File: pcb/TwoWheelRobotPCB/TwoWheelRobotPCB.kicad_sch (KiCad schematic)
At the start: 26 parts, among them J1 Motor1, J2 Motor2, U1 NodeMCU1.0(ESP-12E), U2 L298HN, U3 ACS712xLCTR-05B

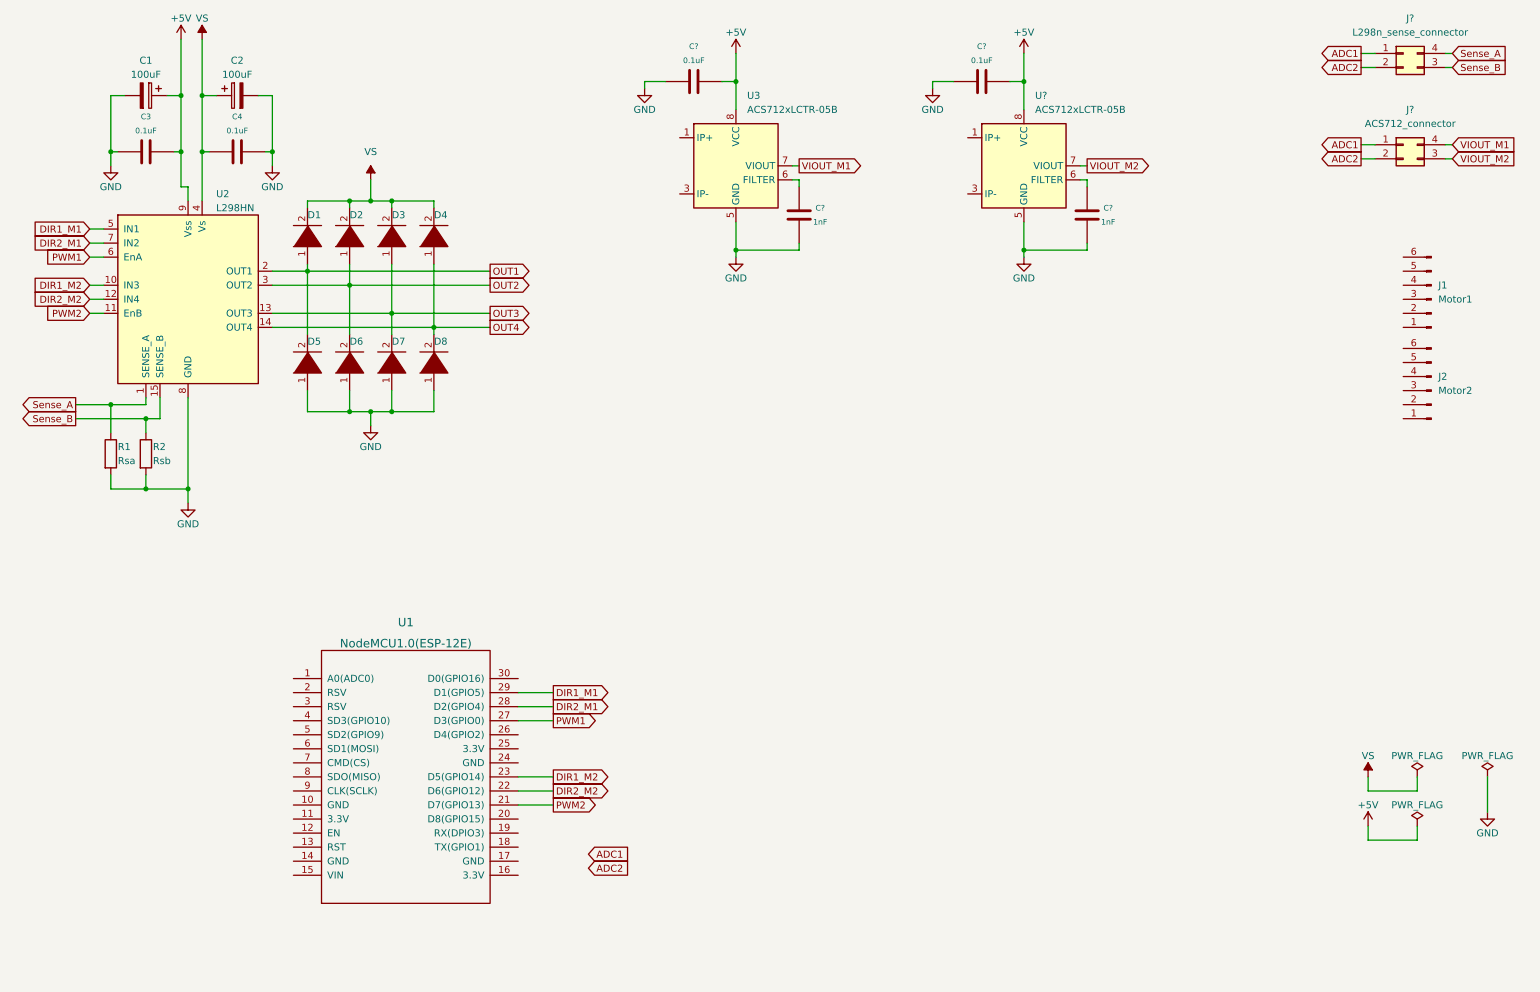
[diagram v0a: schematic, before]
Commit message: robotView class && update pcb
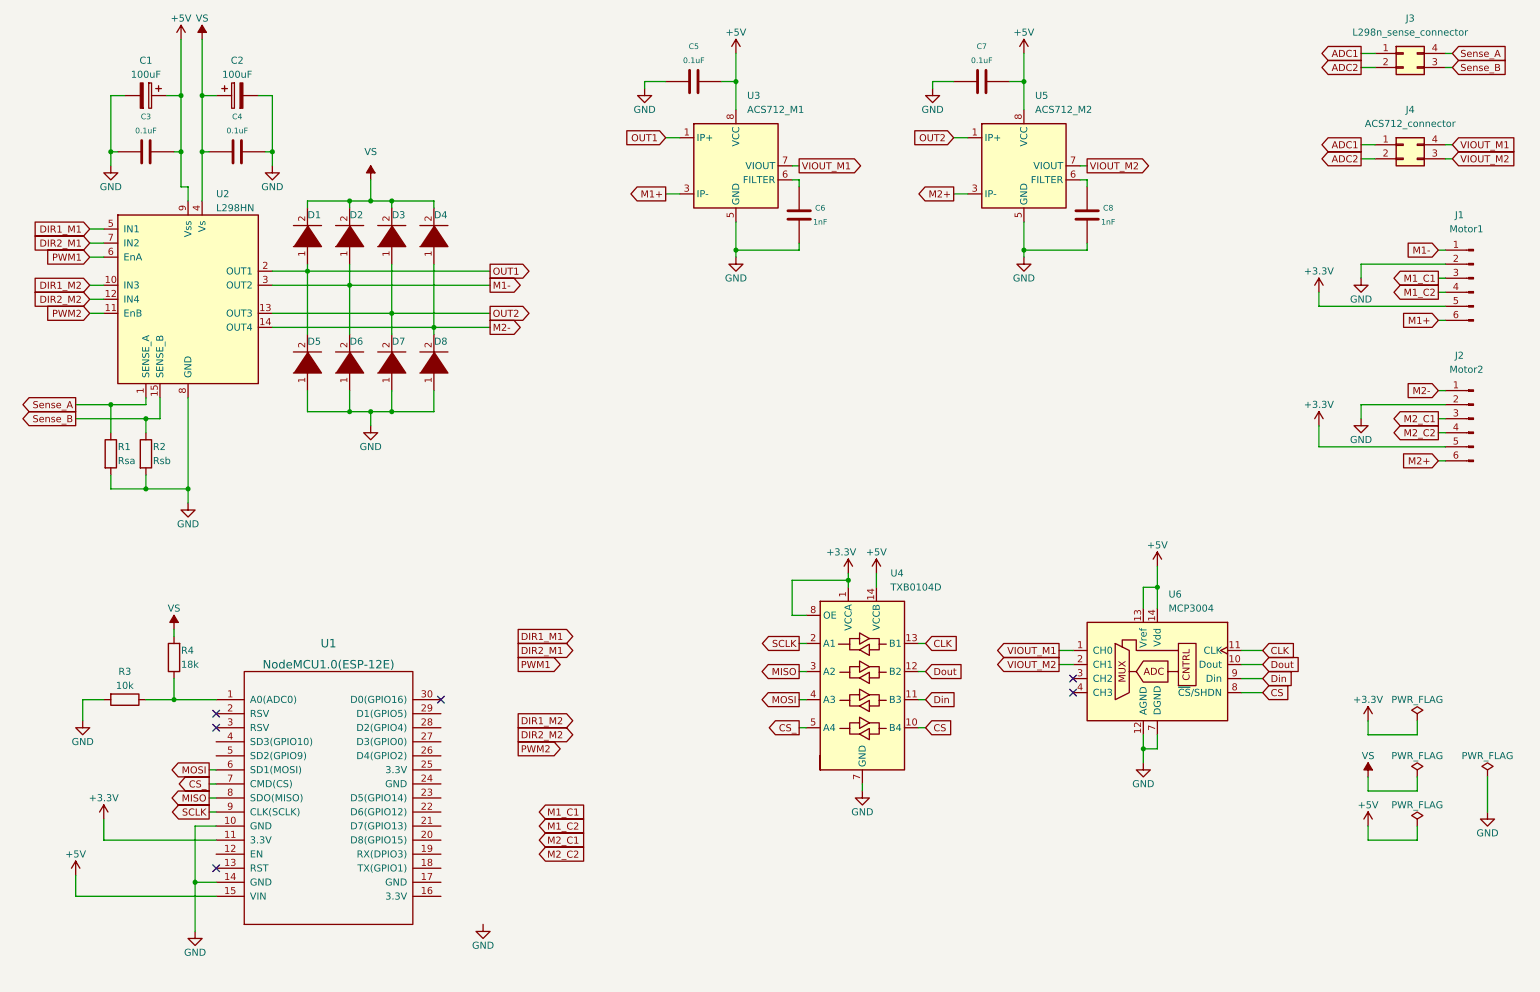
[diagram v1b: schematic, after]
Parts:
- added R3: 10k, symbol Device:R
- added R4: 18k, symbol Device:R
- added U4: TXB0104D, Package_SO:SOIC-14_3.9x8.7mm_P1.27mm, symbol Logic_LevelTranslator:TXB0104D
- added U6: MCP3004, symbol Analog_ADC:MCP3004
- U3: value ACS712xLCTR-05B -> ACS712_M1
- U5: renamed from U?; value ACS712xLCTR-05B -> ACS712_M2
- gave numbers to parts that had none: 6
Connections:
- net OUT3 is gone; now on net OUT2: D3.1 (K), D7.2 (A), U2.13 (OUT3)
- net OUT4 is gone; now on net M2-: D4.1 (K), D8.2 (A), U2.14 (OUT4)
- net +5V: now also U1.15 (VIN), U4.14 (VCCB), U6.13 (Vref), U6.14 (Vdd)
- net DIR1_M1: no longer U1.29 (D1(GPIO5))
- net DIR1_M2: no longer U1.23 (D5(GPIO14))
- net DIR2_M1: no longer U1.28 (D2(GPIO4))
- net DIR2_M2: no longer U1.22 (D6(GPIO12))
- net GND: now also J1.2 (Pin_2), J2.2 (Pin_2), U1.10 (GND), U1.14 (GND), R3.2, U4.7 (GND), U6.12 (AGND), U6.7 (DGND)
- net OUT1: now also U3.1 (IP+), U3.2 (IP+)
- net OUT2: now also U5.1 (IP+), U5.2 (IP+); no longer D2.1 (K), D6.2 (A), U2.3 (OUT2)
- net PWM1: no longer U1.27 (D3(GPIO0))
- net PWM2: no longer U1.21 (D7(GPIO13))
- net VIOUT_M1: now also U6.1 (CH0)
- net VIOUT_M2: now also U6.2 (CH1)
- net VS: now also R4.2
- net at U1.1 (A0(ADC0)): now also R3.1, R4.1
- net +3V3: now reaches U1.11 (3.3V)
- net +3V3: now also J1.5 (Pin_5), J2.5 (Pin_5), U4.1 (VCCA), U4.8 (OE)
- net MOSI: now reaches U1.6 (SD1(MOSI))
- net MOSI: now also U4.4 (A3)
- net CS_: now reaches U1.7 (CMD(CS))
- net CS_: now also U4.5 (A4)
- net MISO: now reaches U1.8 (SDO(MISO))
- net MISO: now also U4.3 (A2)
- net SCLK: now reaches U1.9 (CLK(SCLK))
- net SCLK: now also U4.2 (A1)
- net M2+: now reaches U5.3 (IP-), U5.4 (IP-)
- net M2+: now also J2.6 (Pin_6)
- net M1-: now reaches J1.1 (Pin_1)
- net M1-: now also D2.1 (K), D6.2 (A), U2.3 (OUT2)
- net M1_C1: now reaches J1.3 (Pin_3)
- net M1_C2: now reaches J1.4 (Pin_4)
- net M1+: now reaches J1.6 (Pin_6)
- net M1+: now also U3.3 (IP-), U3.4 (IP-)
- net M2-: now reaches J2.1 (Pin_1)
- net M2_C1: now reaches J2.3 (Pin_3)
- net M2_C2: now reaches J2.4 (Pin_4)
- new net CLK: U4.13 (B1), U6.11 (CLK)
- new net CS: U4.10 (B4), U6.8 (~{CS}/SHDN)
- new net Din: U4.11 (B3), U6.9 (Din)
- new net Dout: U4.12 (B2), U6.10 (Dout)
- no-connect marks 0 -> 6
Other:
- moved on the sheet: J1, J2, U1

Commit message: pcb update
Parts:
- removed C1, C2: 100uF, symbol Device:C_Polarized
- removed C3, C4, C5, C7: 0.1uF, symbol cyclophone:C
- removed C6, C8: 1nF, symbol cyclophone:C
- removed D1, D2, D3, D4, D5, D6, D7, D8: DIODE, symbol pspice:DIODE
- removed J1: Motor1, Connector_PinHeader_2.54mm:PinHeader_1x06_P2.54mm_Vertical, symbol Connector:Conn_01x06_Male
- removed J2: Motor2, Connector_PinHeader_2.54mm:PinHeader_1x06_P2.54mm_Vertical, symbol Connector:Conn_01x06_Male
- removed J3: L298n_sense_connector, Connector_PinHeader_2.54mm:PinHeader_2x02_P2.54mm_Vertical, symbol Connector_Generic:Conn_02x02_Counter_Clockwise
- removed J4: ACS712_connector, Connector_PinHeader_2.54mm:PinHeader_2x02_P2.54mm_Vertical, symbol Connector_Generic:Conn_02x02_Counter_Clockwise
- removed R1: Rsa, symbol Device:R
- removed R2: Rsb, symbol Device:R
- removed U2: L298HN, Package_TO_SOT_THT:TO-220-15_P2.54x2.54mm_StaggerOdd_Lead4.58mm_Vertical, symbol Driver_Motor:L298HN
- removed U3: ACS712_M1, Package_SO:SOIC-8_3.9x4.9mm_P1.27mm, symbol Sensor_Current:ACS712xLCTR-05B
- removed U4: TXB0104D, Package_SO:SOIC-14_3.9x8.7mm_P1.27mm, symbol Logic_LevelTranslator:TXB0104D
- removed U5: ACS712_M2, Package_SO:SOIC-8_3.9x4.9mm_P1.27mm, symbol Sensor_Current:ACS712xLCTR-05B
- removed U6: MCP3004, symbol Analog_ADC:MCP3004
- R3, R4: footprint (none) -> Resistor_SMD:R_0805_2012Metric
- U1: footprint (none) -> NodemcuESP8266_footprint:MODULE_ZC563900
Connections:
- net +3V3: now also U1.16 (3.3V), U1.25 (3.3V)
- net GND: now also U1.17 (GND), U1.24 (GND)
- net M1_C1: now also U1.22 (D6(GPIO12))
- net M1_C2: now also U1.23 (D5(GPIO14))
- net M2_C1: now also U1.21 (D7(GPIO13))
- net M2_C2: now also U1.20 (D8(GPIO15))
- net pwm2: now reaches U1.26 (D4(GPIO2))
- net pwm1: now reaches U1.27 (D3(GPIO0))
- net SDA: now reaches U1.28 (D2(GPIO4))
- net SCL: now reaches U1.29 (D1(GPIO5))
- no-connect marks 6 -> 9
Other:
- added sheet Measurement (Measurement.kicad_sch)
- added sheet MotorDriver (MotorDriver.kicad_sch)
- added sheet Supply (Supply.kicad_sch)
- moved on the sheet: R3, R4, U1

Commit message: update pcb
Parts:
- removed U1: NodeMCU1.0(ESP-12E), NodemcuESP8266_footprint:MODULE_ZC563900, symbol ESP8266:NodeMCU1.0(ESP-12E)
- added U1: ZC563900, NodemcuESP8266_footprint:MODULE_ZC563900, symbol NodemcuV2:ZC563900
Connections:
- net +3V3: now also U1.11 (3V3), U1.16 (3V3), U1.25 (3V3)
- net CS_: now also U1.7 (CMD)
- net GND: now also U1.10 (GND), U1.14 (GND), U1.17 (GND), U1.24 (GND)
- net M1_C1: now also U1.22 (D6)
- net M1_C2: now also U1.23 (D5)
- net M2_C1: now also U1.21 (D7)
- net M2_C2: now also U1.20 (D8)
- net MISO: now also U1.8 (SD0)
- net MOSI: now also U1.6 (SD1)
- net SCL: now also U1.29 (D1)
- net SCLK: now also U1.9 (CLK)
- net SDA: now also U1.28 (D2)
- net VS: now also U1.15 (VIN)
- net pwm1: now also U1.27 (D3)
- net pwm2: now also U1.26 (D4)
- net at R3.1, R4.1: now also U1.1 (A0)
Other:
- moved on the sheet: R3, R4

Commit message: pcb
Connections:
- net pwm1 renamed pwm1_3v3
- net pwm2 renamed pwm2_3v3
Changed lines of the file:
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@@
     )
   )
-  (global_label "pwm2" (shape output) (at 111.76 69.85 0) (fields_autoplaced)
+  (global_label "pwm2_3v3" (shape output) (at 111.76 69.85 0) (fields_autoplaced)
     (effects (font (size 1.27 1.27)) (justify left))
-    (property "Intersheet References" "${INTERSHEET_REFS}" (id 0) (at 119.5555 69.7706 0)
+    (property "Intersheet References" "${INTERSHEET_REFS}" (id 0) (at 123.9098 69.7706 0)
       (effects (font (size 1.27 1.27)) (justify left) hide)
     )
@@
     )
   )
-  (global_label "pwm1" (shape output) (at 111.76 67.31 0) (fields_autoplaced)
+  (global_label "pwm1_3v3" (shape output) (at 111.76 67.31 0) (fields_autoplaced)
     (effects (font (size 1.27 1.27)) (justify left))
-    (property "Intersheet References" "${INTERSHEET_REFS}" (id 0) (at 119.5555 67.2306 0)
+    (property "Intersheet References" "${INTERSHEET_REFS}" (id 0) (at 123.9098 67.2306 0)
       (effects (font (size 1.27 1.27)) (justify left) hide)
     )
@@
       (reference "#FLG04") (unit 1) (value "PWR_FLAG") (footprint "")
     )
+    (path "/7d587865-2231-4a38-9d8a-97d485f2f4e4/4c8df18d-77ed-4411-bc03-a1485170a702"
+      (reference "#PWR01") (unit 1) (value "VS") (footprint "")
+    )
     (path "/a80922d8-842d-4acc-a603-f8902aa0c0c5"
       (reference "#PWR02") (unit 1) (value "GND") (footprint "")
     )
+    (path "/7d587865-2231-4a38-9d8a-97d485f2f4e4/984e7252-4d51-4e18-8cfd-d20f5368238e"
+      (reference "#PWR03") (unit 1) (value "GND") (footprint "")
+    )
+    (path "/7d587865-2231-4a38-9d8a-97d485f2f4e4/cbc1633b-2edb-4841-a64c-00ea63fa9a87"
+      (reference "#PWR04") (unit 1) (value "VS") (footprint "")
+    )
     (path "/bab16bbd-be5b-4ff6-9805-0a16f023b621"
       (reference "#PWR05") (unit 1) (value "VS") (footprint "")
     )
+    (path "/7d587865-2231-4a38-9d8a-97d485f2f4e4/df76744a-2672-4df3-b0f1-8632a1e0c956"
+      (reference "#PWR06") (unit 1) (value "GND") (footprint "")
+    )
+    (path "/7d587865-2231-4a38-9d8a-97d485f2f4e4/15eb6ae6-6d8f-499f-a0b3-7ad0e61d54f9"
+      (reference "#PWR07") (unit 1) (value "GND") (footprint "")
+    )
     (path "/5d98914d-1801-43c8-96ca-19f222dbae40/43f9481c-710c-4a70-b5b4-8f4b24641629"
       (reference "#PWR08") (unit 1) (value "GND") (footprint "")
@@
       (reference "#PWR011") (unit 1) (value "VS") (footprint "")
     )
+    (path "/7d587865-2231-4a38-9d8a-97d485f2f4e4/d045e7ba-b7a5-4eb8-ba31-1a87a3b8ae7d"
+      (reference "#PWR012") (unit 1) (value "+5V") (footprint "")
+    )
     (path "/5d98914d-1801-43c8-96ca-19f222dbae40/30c9f8d1-6270-4c18-a2b6-c43a30582ae1"
       (reference "#PWR013") (unit 1) (value "GND") (footprint "")
@@
       (reference "#PWR019") (unit 1) (value "GND") (footprint "")
     )
-    (path "/5d98914d-1801-43c8-96ca-19f222dbae40/47165815-d55a-454b-961f-9380e65de16a"
+    (path "/5d98914d-1801-43c8-96ca-19f222dbae40/e3cbd370-7c22-4222-878e-9ad9b35baaf2"
       (reference "#PWR020") (unit 1) (value "+3.3V") (footprint "")
     )
-    (path "/5d98914d-1801-43c8-96ca-19f222dbae40/e457ae7e-3438-4d1d-a954-7f6d6264bc05"
-      (reference "#PWR021") (unit 1) (value "GND") (footprint "")
-    )
-    (path "/5d98914d-1801-43c8-96ca-19f222dbae40/d657a5c7-f508-4351-b8c0-caf046b97c66"
-      (reference "#PWR022") (unit 1) (value "+5V") (footprint "")
+    (path "/5d98914d-1801-43c8-96ca-19f222dbae40/11b85eea-dc35-46a9-96f1-4b1e7636e86a"
+      (reference "#PWR021") (unit 1) (value "+3.3V") (footprint "")
+    )
+    (path "/5d98914d-1801-43c8-96ca-19f222dbae40/2bf65490-bdce-49a7-b615-e71bdc3e6432"
+      (reference "#PWR022") (unit 1) (value "GND") (footprint "")
     )
     (path "/5d98914d-1801-43c8-96ca-19f222dbae40/446365ea-1547-4ab1-9f38-dd7104295afb"
@@
       (reference "#PWR041") (unit 1) (value "GND") (footprint "")
     )
+    (path "/5d98914d-1801-43c8-96ca-19f222dbae40/fd4dabcb-18d2-466b-b827-05bda2ed2a9c"
+      (reference "#PWR042") (unit 1) (value "+5V") (footprint "")
+    )
     (path "/1862457e-eb7f-42c4-b8ca-a4b27406c6d7"
       (reference "#PWR0101") (unit 1) (value "GND") (footprint "")
@@
       (reference "C8") (unit 1) (value "1nF") (footprint "Capacitor_SMD:C_0805_2012Metric")
     )
+    (path "/7d587865-2231-4a38-9d8a-97d485f2f4e4/8c56c79c-7af4-40fc-8d6c-2391d30538c4"
+      (reference "C9") (unit 1) (value "100uF") (footprint "Capacitor_THT:CP_Radial_D6.3mm_P2.50mm")
+    )
+    (path "/7d587865-2231-4a38-9d8a-97d485f2f4e4/90f4a887-faea-4c69-a0af-0d8fe86d677c"
+      (reference "C10") (unit 1) (value "0.1uF") (footprint "Capacitor_THT:C_Disc_D4.3mm_W1.9mm_P5.00mm")
+    )
+    (path "/7d587865-2231-4a38-9d8a-97d485f2f4e4/21a0e9c8-dee6-4f28-bdc4-f2405df583e6"
+      (reference "C11") (unit 1) (value "680uF") (footprint "Capacitor_SMD:CP_Elec_8x6.9")
+    )
+    (path "/7d587865-2231-4a38-9d8a-97d485f2f4e4/0ae213ea-5f39-486e-886a-e2700d74a572"
+      (reference "C12") (unit 1) (value "220uF") (footprint "Capacitor_SMD:CP_Elec_8x6.9")
+    )
     (path "/5d98914d-1801-43c8-96ca-19f222dbae40/ea2db8f6-2cca-4218-9b19-60965fcb02ed"
       (reference "D1") (unit 1) (value "DIODE") (footprint "Diode_THT:D_A-405_P10.16mm_Horizontal")
@@
       (reference "D8") (unit 1) (value "DIODE") (footprint "Diode_THT:D_A-405_P10.16mm_Horizontal")
     )
+    (path "/7d587865-2231-4a38-9d8a-97d485f2f4e4/52ef34a6-f506-464a-95e4-48addca555bc"
+      (reference "D9") (unit 1) (value "1N5825") (footprint "Diode_SMD:D_2010_5025Metric_Pad1.52x2.65mm_HandSolder")
+    )
     (path "/5d98914d-1801-43c8-96ca-19f222dbae40/ad439bee-fa7a-4275-9dda-be9562a285ae"
-      (reference "J3") (unit 1) (value "Motor1") (footprint "Connector_PinHeader_2.54mm:PinHeader_1x06_P2.54mm_Vertical")
+      (reference "J1") (unit 1) (value "Motor1") (footprint "Connector_PinHeader_2.54mm:PinHeader_1x06_P2.54mm_Vertical")
     )
     (path "/5d98914d-1801-43c8-96ca-19f222dbae40/42d8d183-8a6d-45ba-a12d-bbab6eb9317f"
-      (reference "J4") (unit 1) (value "Motor2") (footprint "Connector_PinHeader_2.54mm:PinHeader_1x06_P2.54mm_Vertical")
+      (reference "J2") (unit 1) (value "Motor2") (footprint "Connector_PinHeader_2.54mm:PinHeader_1x06_P2.54mm_Vertical")
+    )
+    (path "/7d587865-2231-4a38-9d8a-97d485f2f4e4/b0999983-8823-4164-8436-8bf2e6297058"
+      (reference "J3") (unit 1) (value "POWER") (footprint "TerminalBlock_RND:TerminalBlock_RND_205-00001_1x02_P5.00mm_Horizontal")
+    )
+    (path "/7d587865-2231-4a38-9d8a-97d485f2f4e4/5379c07b-65c8-4496-8da0-933e8b8a86a5"
+      (reference "J4") (unit 1) (value "XT60-M") (footprint "footprint:AMASS_XT60-M")
+    )
+    (path "/7d587865-2231-4a38-9d8a-97d485f2f4e4/c665d5f5-cfa3-4d27-ba71-29f466dc52e9"
+      (reference "L1") (unit 1) (value "33uH") (footprint "Inductor_SMD:L_Bourns_SRP1245A")
     )
     (path "/5d98914d-1801-43c8-96ca-19f222dbae40/e6024f9f-8e68-45e7-a471-d53cf11ecf66"
@@
       (reference "R6") (unit 1) (value "2k2") (footprint "Resistor_SMD:R_0805_2012Metric")
     )
+    (path "/7d587865-2231-4a38-9d8a-97d485f2f4e4/1495b4af-d2d5-4440-8b78-75857f825242"
+      (reference "SW1") (unit 1) (value "SW_DPDT_x2") (footprint "Button_Switch_THT:SW_PUSH_E-Switch_FS5700DP_DPDT")
+    )
     (path "/ec062509-e43d-478c-ad0a-4deb2e0e42c0"
       (reference "U1") (unit 1) (value "ZC563900") (footprint "NodemcuESP8266_footprint:MODULE_ZC563900")
@@
       (reference "U3") (unit 1) (value "PCF8574") (footprint "PCF8574:SO16W")
     )
-    (path "/5d98914d-1801-43c8-96ca-19f222dbae40/8af2360a-9a89-4a36-a9b6-da5a660b1e19"
-      (reference "U4") (unit 1) (value "TXB0108DQSR") (footprint "TXB0108_TSOP20_fotprint:SOP65P640X120-20N")
+    (path "/5d98914d-1801-43c8-96ca-19f222dbae40/cd676e39-8b0b-4a97-a5f7-f1a894ba4f9c"
+      (reference "U4") (unit 1) (value "TXB0108PWR") (footprint "TXB0108_TSOP20_fotprint:SOP65P640X120-20N")
     )
     (path "/4f34e6bd-8488-4666-87ea-d049bdfdbeee/1c670057-d2d9-4caa-afa0-cbbef1da2910"
@@
       (reference "U8") (unit 1) (value "ACS712_M2") (footprint "Package_SO:SOIC-8_3.9x4.9mm_P1.27mm")
     )
-  )
+    (path "/7d587865-2231-4a38-9d8a-97d485f2f4e4/faecffa1-e510-4609-90b1-ec816da7b5c8"
+      (reference "U9") (unit 1) (value "LM2596S-5") (footprint "Package_TO_SOT_SMD:TO-263-5_TabPin3")
+    )
+  )

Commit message: pcb finish
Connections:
- net VS: no longer U1.15 (VIN)
- new net +5V: U1.15 (VIN)
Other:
- moved on the sheet: R3, R4
